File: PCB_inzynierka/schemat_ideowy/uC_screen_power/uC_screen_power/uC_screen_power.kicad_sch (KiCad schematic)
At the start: 13 parts, among them J1 Barrel_Jack_Switch, SW73 SW_DPST, SW74 SW_DPST, SW75 SW_DPST, SW76 SW_DPST, U10 TFT_320x240, U11 NUCLEO-F401RE

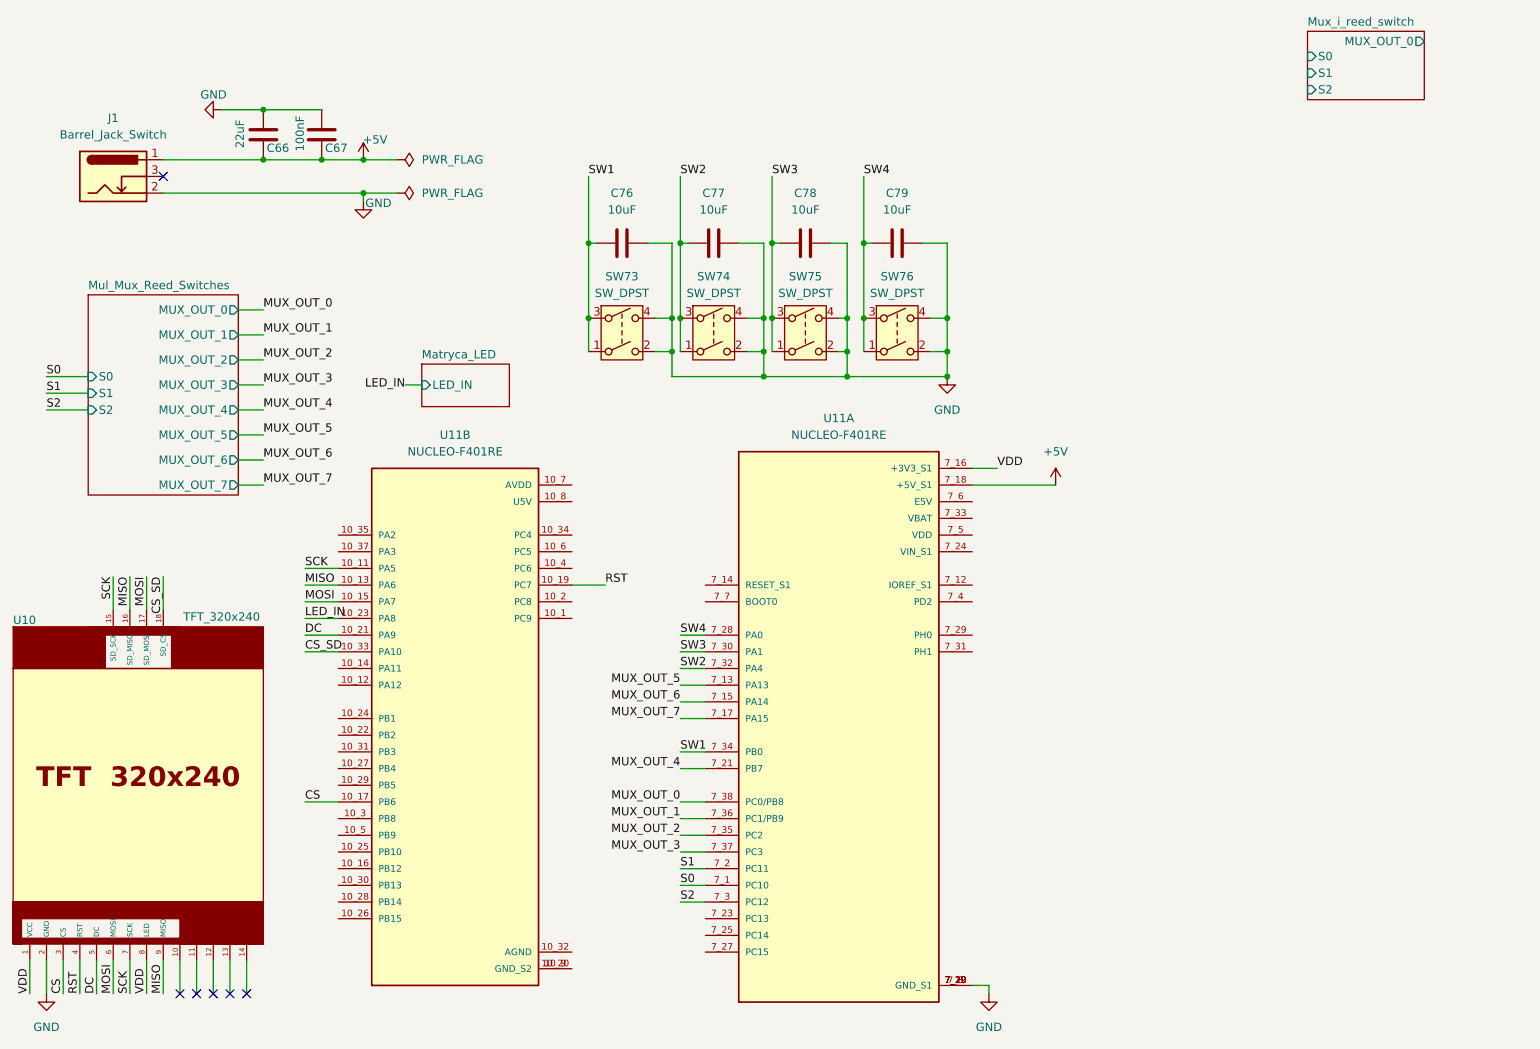
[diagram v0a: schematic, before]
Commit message: plytka 4x4 zawierajaca mux, reed switche i ledy argb v1.0
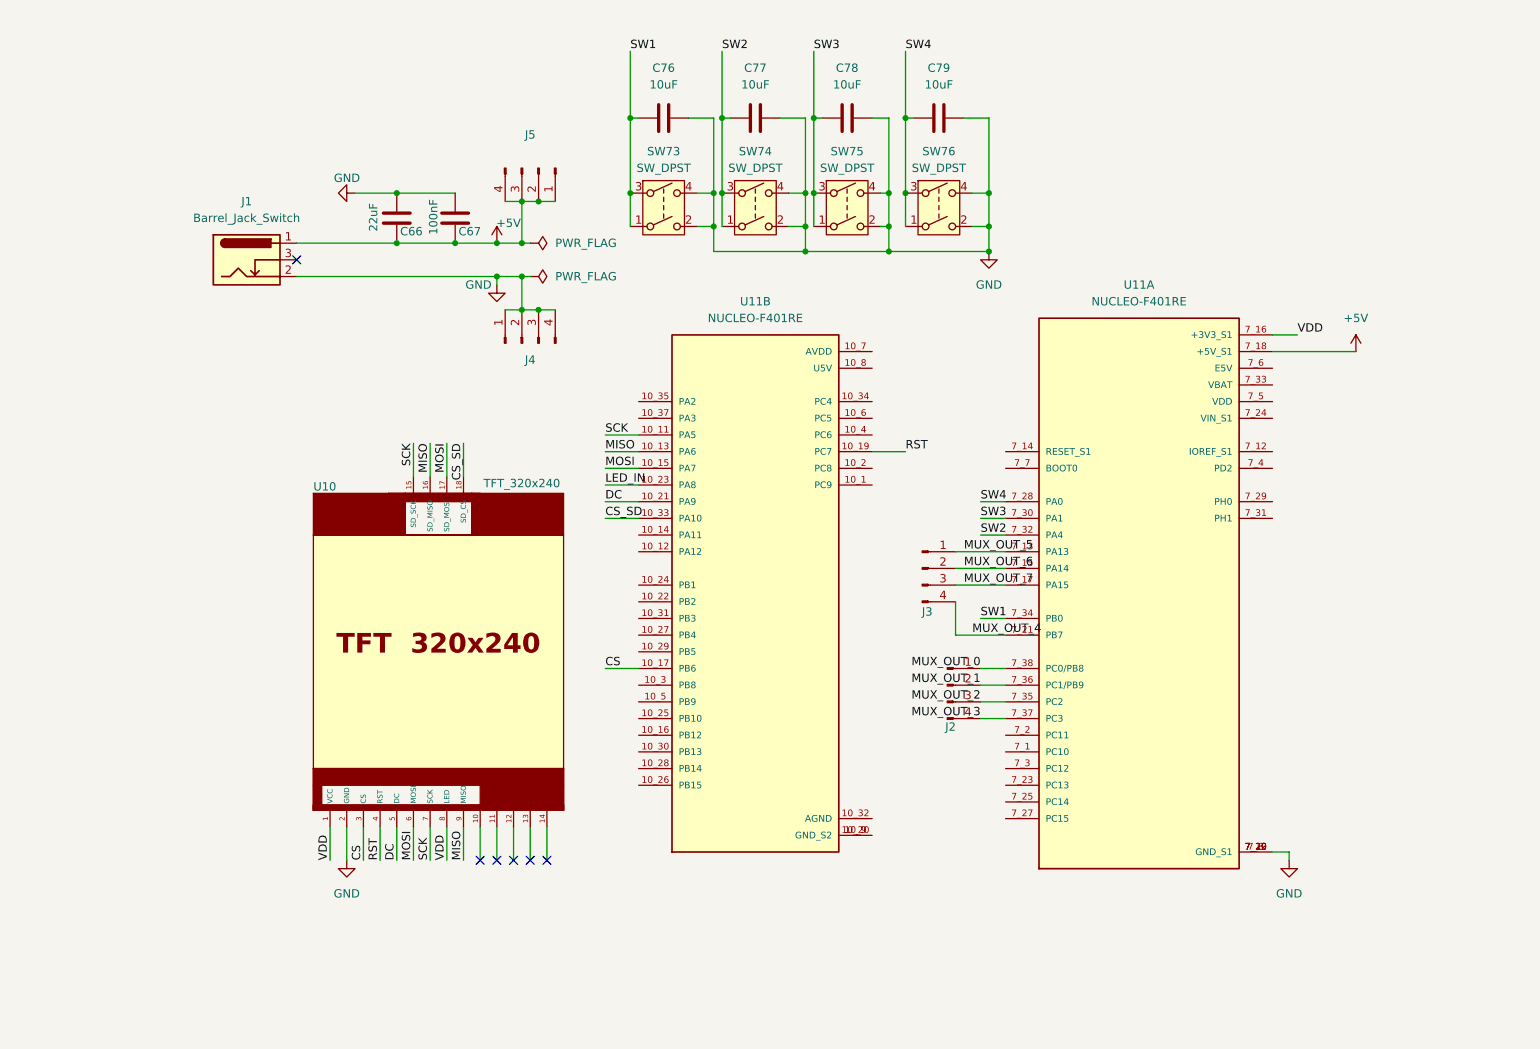
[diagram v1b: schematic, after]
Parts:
- added J2, J3: Conn_01x04_Pin, Connector_PinHeader_2.54mm:PinHeader_1x04_P2.54mm_Vertical, symbol Connector:Conn_01x04_Pin
- added J4, J5: Conn_01x04_Pin, Connector_PinHeader_2.54mm:PinHeader_1x04_P2.54mm_Horizontal, symbol Connector:Conn_01x04_Pin
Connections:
- net +5V: now also J5.1 (Pin_1), J5.2 (Pin_2), J5.3 (Pin_3), J5.4 (Pin_4)
- net GND: now also J4.1 (Pin_1), J4.2 (Pin_2), J4.3 (Pin_3), J4.4 (Pin_4)
- net MUX_OUT_0: now also J2.1 (Pin_1)
- net MUX_OUT_1: now also J2.2 (Pin_2)
- net MUX_OUT_2: now also J2.3 (Pin_3)
- net MUX_OUT_3: now also J2.4 (Pin_4)
- net MUX_OUT_4: now also J3.4 (Pin_4)
- net MUX_OUT_5: now also J3.1 (Pin_1)
- net MUX_OUT_6: now also J3.2 (Pin_2)
- net MUX_OUT_7: now also J3.3 (Pin_3)
- net S0: no longer names the net of U11.7_1 (PC10)
- net S1: no longer names the net of U11.7_2 (PC11)
- net S2: no longer names the net of U11.7_3 (PC12)
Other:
- removed sheet Matryca_LED
- removed sheet Mul_Mux_Reed_Switches
- removed sheet Mux_i_reed_switch
- moved on the sheet: C66, C67, C76, C77, C78, C79, J1, SW73, SW74, SW75, SW76, U10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

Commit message: obie plytki pcb przygotowane, schematy ideowe opisane
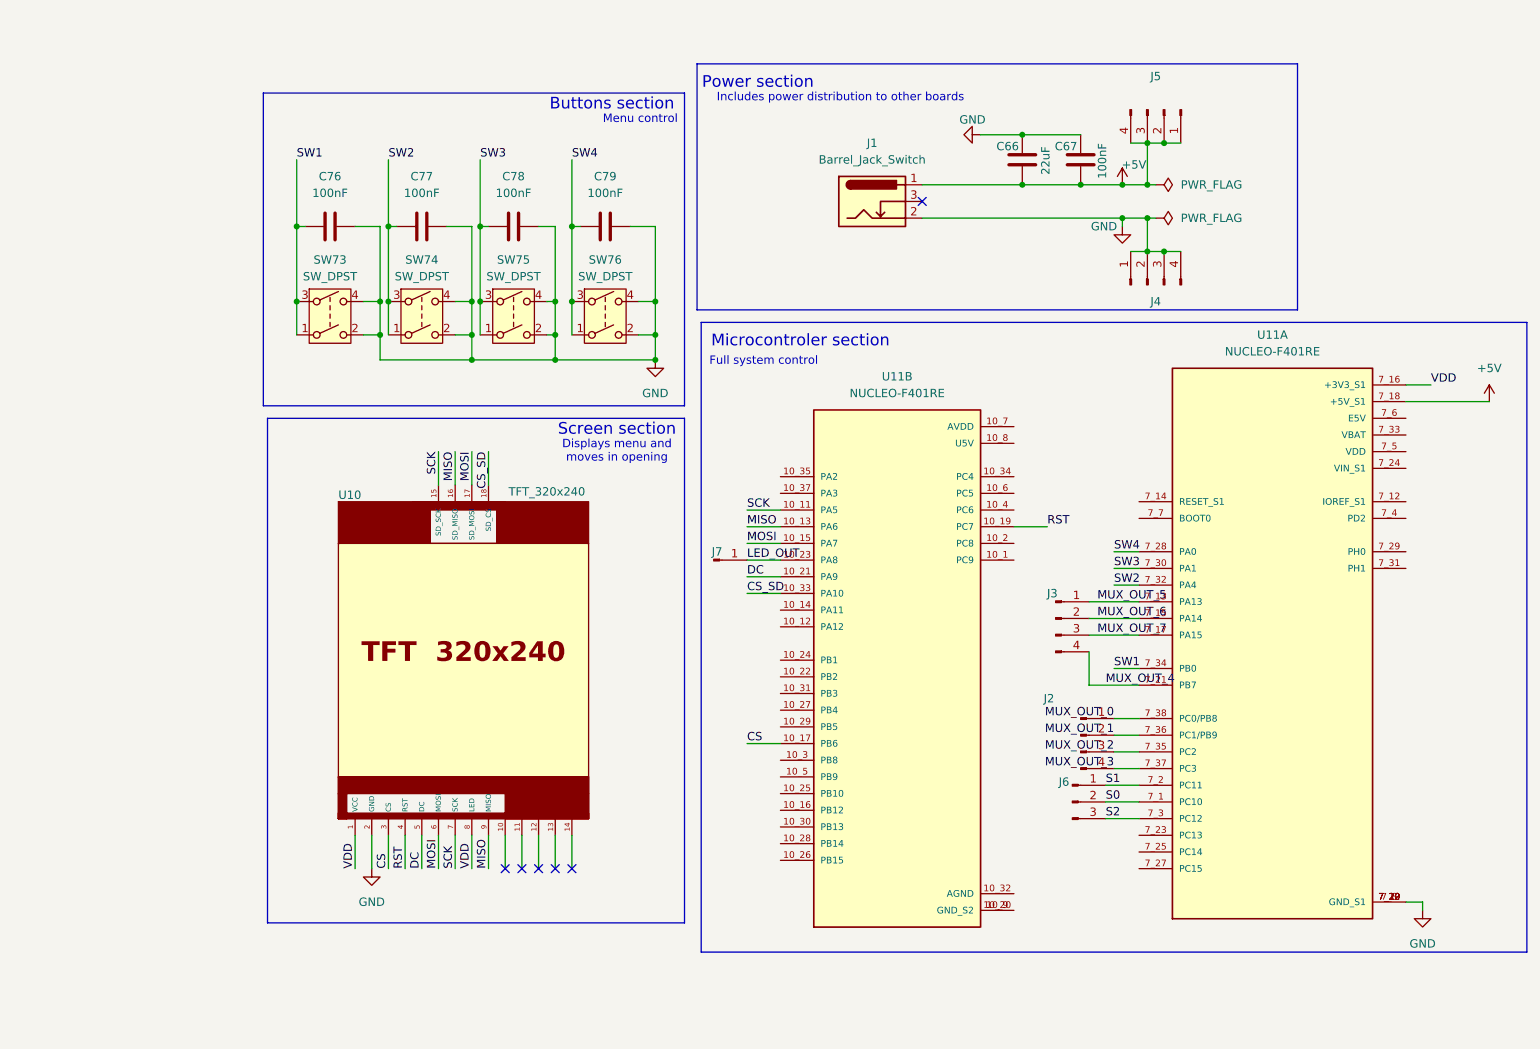
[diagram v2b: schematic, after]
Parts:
- added J6: Conn_01x03_Pin, Connector_PinHeader_2.54mm:PinHeader_1x03_P2.54mm_Vertical, symbol Connector:Conn_01x03_Pin
- added J7: Conn_01x01_Pin, Connector_PinHeader_2.54mm:PinHeader_1x01_P2.54mm_Vertical, symbol Connector:Conn_01x01_Pin
- C76, C77, C78, C79: value 10uF -> 100nF
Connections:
- net +5V: now also C66.1, C67.1; no longer C66.2, C67.2
- net GND: now also C66.2, C67.2; no longer C66.1, C67.1
- net S0: now reaches U11.7_1 (PC10)
- net S0: now also J6.2 (Pin_2)
- net S1: now reaches U11.7_2 (PC11)
- net S1: now also J6.1 (Pin_1)
- net S2: now reaches U11.7_3 (PC12)
- net S2: now also J6.3 (Pin_3)
- net LED_IN renamed LED_OUT
- net LED_OUT: now also J7.1 (Pin_1)
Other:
- note added: "Buttons section"
- note added: "Displays menu and moves in opening"
- note added: "Full system control"
- note added: "Includes power distribution to other boards"
- note added: "Menu control"
- note added: "Microcontroler section"
- note added: "Power section"
- note added: "Screen section"
- company: (none) -> AGH
- title: (none) -> Mikrokontroler, przyciski, wyswietlacz i sekcja zasilania
- moved on the sheet: C66, C67, C76, C77, C78, C79, J1, J2, J3, J4, J5, SW73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
